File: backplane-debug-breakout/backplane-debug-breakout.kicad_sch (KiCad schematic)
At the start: 11 parts, among them J1 Conn_02x08_Odd_Even, J2 Conn_01x04, J3 Conn_01x01_Socket, J4 Conn_01x01_Socket, J5 Conn_01x04, SW1 SW_Push, SW2 SW_DPST_x2, U1 UMFT234XF

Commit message: modified pcb
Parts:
- removed SW1: SW_Push, oresat-misc:D6R90_CNK, symbol Switch:SW_Push
- removed SW2: SW_DPST_x2, Connector_PinHeader_2.54mm:PinHeader_1x03_P2.54mm_Vertical, symbol Switch:SW_DPST_x2
- added SW2: SW_Omron_B3FS, Button_Switch_THT:SW_PUSH_6mm, symbol Switch:SW_Omron_B3FS
- added SW3: EG1218, Connector_PinHeader_2.54mm:PinHeader_1x03_P2.54mm_Vertical, symbol Switch:SW_SPDT_321
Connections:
- net GND: now also SW2.1, SW3.1 (C)
- net SD: now also SW2.2, SW3.2 (B)
- net VBUS: now reaches F1.1, J1.10 (Pin_10), J1.6 (Pin_6), J1.8 (Pin_8)
- no-connect marks 8 -> 11
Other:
- note added: "Banana jacks for external power"
- note added: "Oresat backplane 16-pin connector"
- note added: "USB to UART adapter daughterboard to debug pc via micro-usb"
- note added: "add spacing to pins"
- note added: "momentary button and slide switch for ~{SHUTDOWN}"
- note added: "not used"
- note added: "vulCAN USB to CAN adapter to debug pc via USB-C"
- note removed: "To vulCAN"
- note removed: "check switch footprints"
- title: (none) -> Backplane Debug Breakout
- moved on the sheet: D1, F1, F2, J1, J2, J3, J4, J5, U1

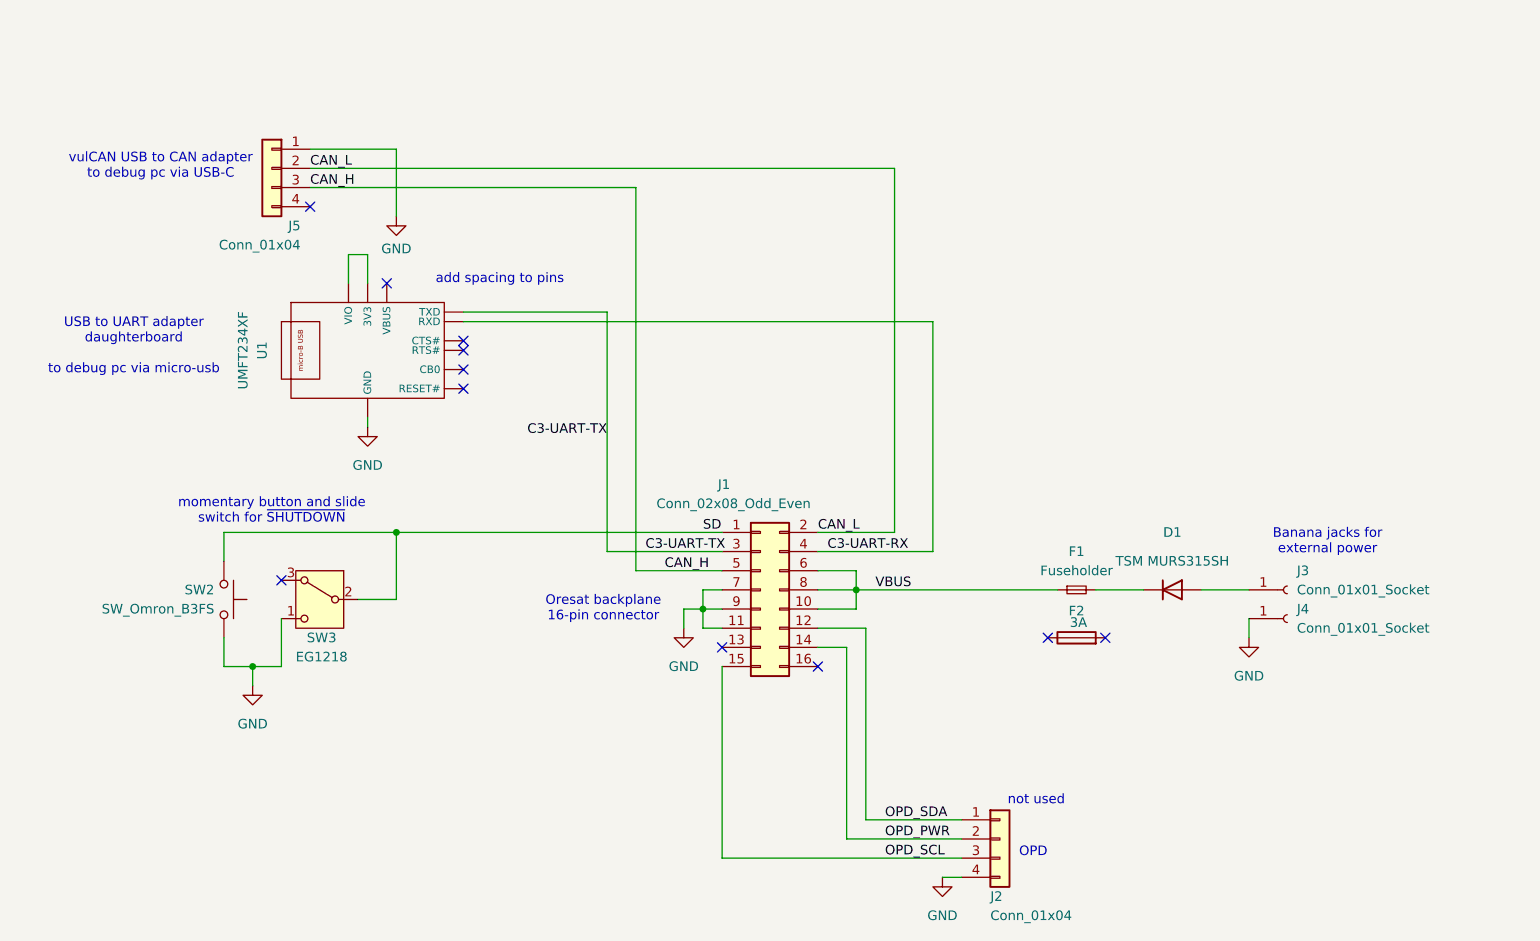
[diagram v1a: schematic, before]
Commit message: Random clean, including some value changes, and moving the vulcan connector around to minimize wire lengths.
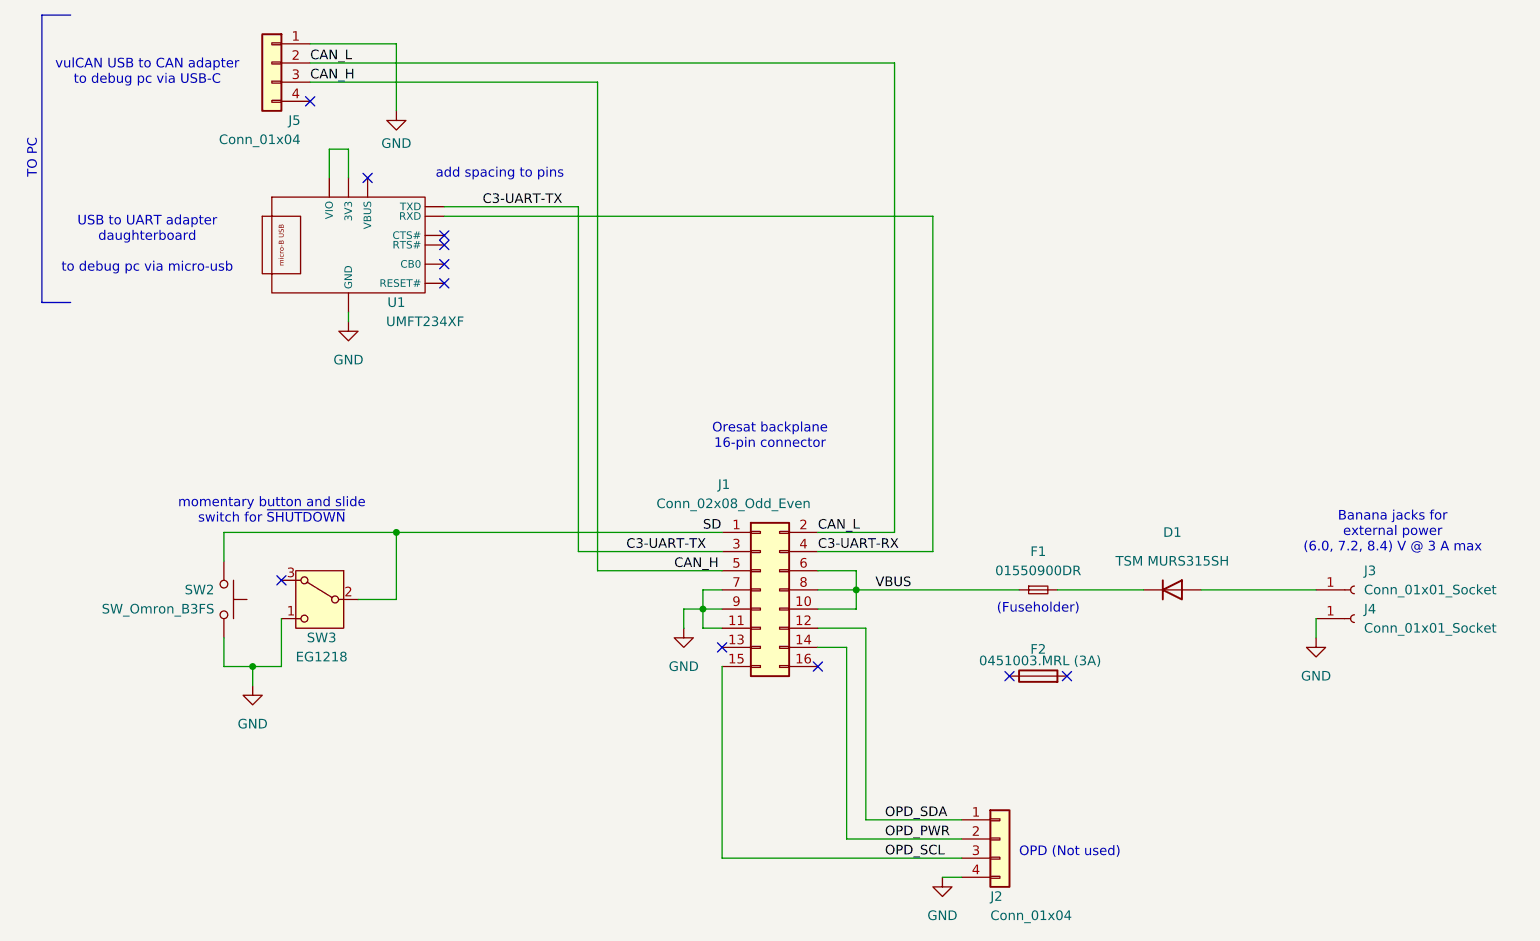
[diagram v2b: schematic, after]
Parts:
- F1: value Fuseholder -> 01550900DR
- F2: value 3A -> 0451003.MRL (3A)
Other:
- note added: "(Fuseholder)"
- note added: "Banana jacks for external power (6.0, 7.2, 8.4) V @ 3 A max"
- note added: "OPD (Not used)"
- note added: "TO PC"
- note removed: "Banana jacks for external power"
- note removed: "OPD"
- note removed: "not used"
- moved on the sheet: F1, F2, J3, J4, J5, U1

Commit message: updated BOM
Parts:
- D1: DST (none) -> Digi-Key; MFR (none) -> TSM
- F1, F2: DST (none) -> Digi-Key; MFR (none) -> LittelFuse
- J1: DPN 609-86130161014345E1LF-ND -> H3DDH-1611618G-ND; DST (none) -> Digi-Key; MFR (none) -> Assman; MPN 86130161014345E1LF -> H3DDH-161618G
- J2: DST (none) -> Digi-Key; now not fitted; now left out of the parts list
- J3: DPN (none) -> 36-7006-ND; DST (none) -> Digi-Key; MFR (none) -> KEYSTONE; MPN (none) -> 7006
- J4: DPN (none) -> 36-7007-ND; DST (none) -> Digi-Key; MFR (none) -> KEYSTONE; MPN (none) -> 7007
- J5: DST (none) -> Digi-Key
- SW2: DPN (none) -> SW400-ND; DST (none) -> Digi-Key; MFR (none) -> Omron; MPN (none) -> B3F-1000
- SW3: DPN (none) -> EG1903-ND; DST (none) -> Digi-Key; MFR (none) -> E-Switch; MPN (none) -> EG1218
- U1: DST (none) -> Digi-Key; MFR (none) -> FTDI, Future Technology Devices International Ltd

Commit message: edited BOM
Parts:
- J1: DPN H3DDH-1611618G-ND -> 732-2095-ND; MFR Assman -> Würth Elektronik; MPN H3DDH-161618G -> 61201621621
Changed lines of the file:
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@@
 			)
 		)
-		(property "Description" "16-position cable assembly socket"
+		(property "Description" "CONN HEADER VERT 16POS 2.54MM Y - 0"
 			(at 144.78 97.79 0)
 			(effects
@@
 			)
 		)
-		(property "DPN" "H3DDH-1611618G-ND"
+		(property "DPN" "732-2095-ND"
 			(at 144.78 97.79 0)
 			(effects
@@
 			)
 		)
-		(property "MPN" "H3DDH-161618G"
+		(property "MPN" "61201621621"
 			(at 144.78 97.79 0)
 			(effects
@@
 			)
 		)
-		(property "MFR" "Assman"
+		(property "MFR" "Würth Elektronik"
 			(at 144.78 97.79 0)
 			(effects

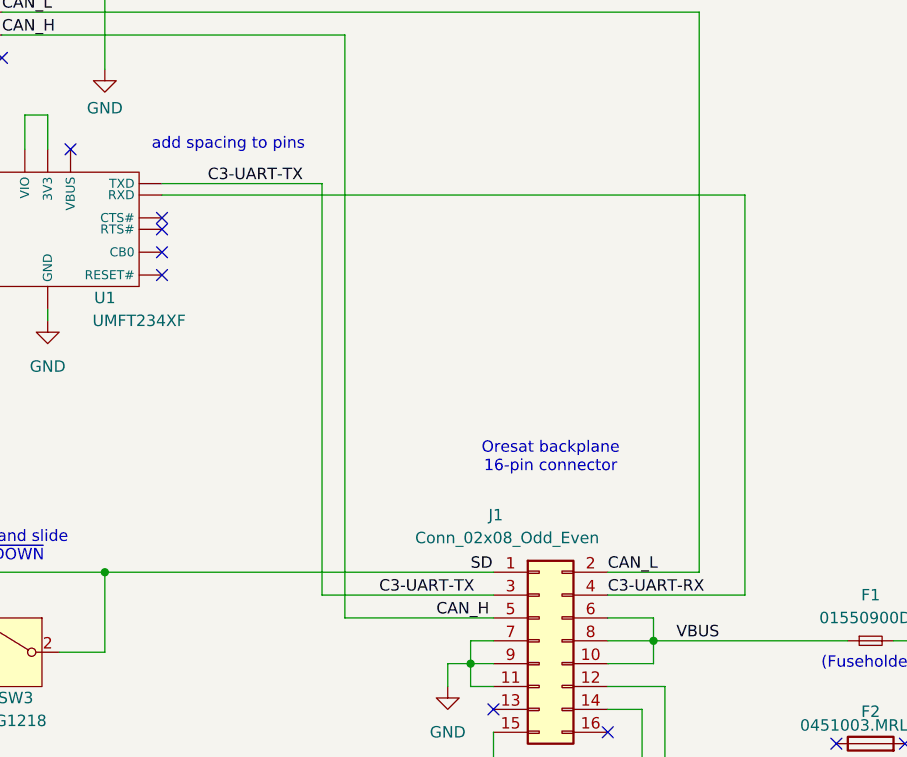
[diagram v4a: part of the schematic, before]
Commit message: fixed tx-rx connections
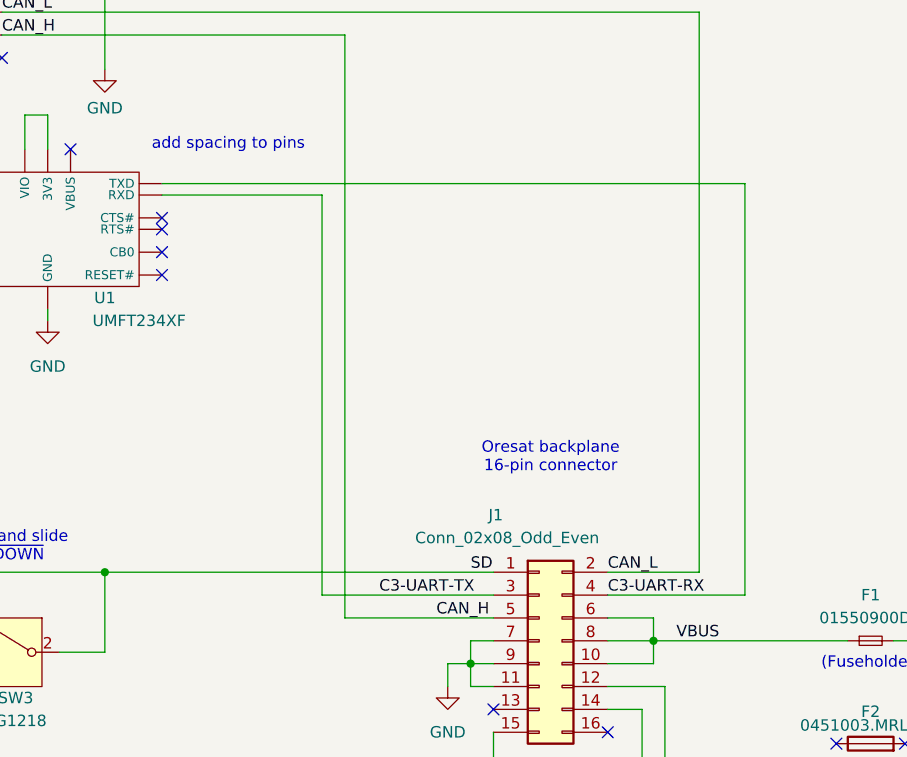
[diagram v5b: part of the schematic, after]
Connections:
- net C3-UART-RX: now also U1.P7 (TXD); no longer U1.P9 (RXD)
- net C3-UART-TX: now also U1.P9 (RXD); no longer U1.P7 (TXD)
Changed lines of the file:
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@@
 	(wire
 		(pts
-			(xy 120.65 46.99) (xy 120.65 92.71)
+			(xy 167.64 46.99) (xy 102.87 46.99)
+		)
+		(stroke
+			(width 0)
+			(type default)
+		)
+	)
+	(wire
+		(pts
+			(xy 120.65 48.26) (xy 102.87 48.26)
 		)
 		(stroke
@@
 	(wire
 		(pts
-			(xy 102.87 46.99) (xy 120.65 46.99)
-		)
-		(stroke
-			(width 0)
-			(type default)
-		)
-	)
-	(wire
-		(pts
 			(xy 137.16 100.33) (xy 137.16 102.87)
 		)
@@
 	(wire
 		(pts
+			(xy 120.65 92.71) (xy 120.65 48.26)
+		)
+		(stroke
+			(width 0)
+			(type default)
+		)
+	)
+	(wire
+		(pts
 			(xy 168.91 135.89) (xy 171.45 135.89)
 		)
@@
 	(wire
 		(pts
-			(xy 167.64 48.26) (xy 102.87 48.26)
-		)
-		(stroke
-			(width 0)
-			(type default)
-		)
-	)
-	(wire
-		(pts
 			(xy 162.56 90.17) (xy 162.56 27.94)
 		)
@@
 	(wire
 		(pts
-			(xy 167.64 92.71) (xy 167.64 48.26)
+			(xy 167.64 46.99) (xy 167.64 92.71)
 		)
 		(stroke
@@
 		(fields_autoplaced yes)
 		(effects
-			(font
-				(size 1.27 1.27)
-			)
-			(justify left bottom)
-		)
-	)
-	(label "C3-UART-TX"
-		(at 107.95 46.99 0)
-		(fields_autoplaced yes)
-		(effects

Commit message: updated schematic
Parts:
- added C1: C, symbol Device:C
- added J6: 629105150521, Connector_USB:USB_Micro-B_Wuerth_629105150521_CircularHoles, symbol Connector:USB_B_Micro
- added SW1: SW_Push_DPDT, symbol Switch:SW_Push_DPDT
- added TP1: TestPoint, symbol Connector:TestPoint
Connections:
- net C3-UART-RX: now also SW1.5 (B); no longer U1.P7 (TXD)
- net C3-UART-TX: now also SW1.2 (B); no longer U1.P9 (RXD)
- net GND: now also C1.2, J6.5 (GND)
- new net: SW1.1 (A), U1.P9 (RXD)
- new net: J6.2 (D-), SW1.3 (C)
- new net: SW1.4 (A), U1.P7 (TXD)
- new net: J6.3 (D+), SW1.6 (C)
- new net: C1.1, J6.6 (Shield)
- new net: J6.1 (VBUS), TP1.1
- no-connect marks 11 -> 12

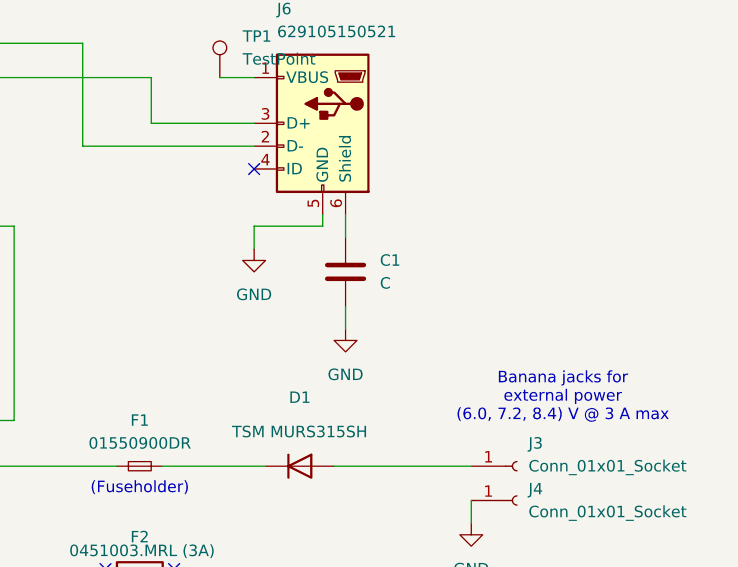
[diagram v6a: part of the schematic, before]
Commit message: added usb-serial connector to schematic and pcb
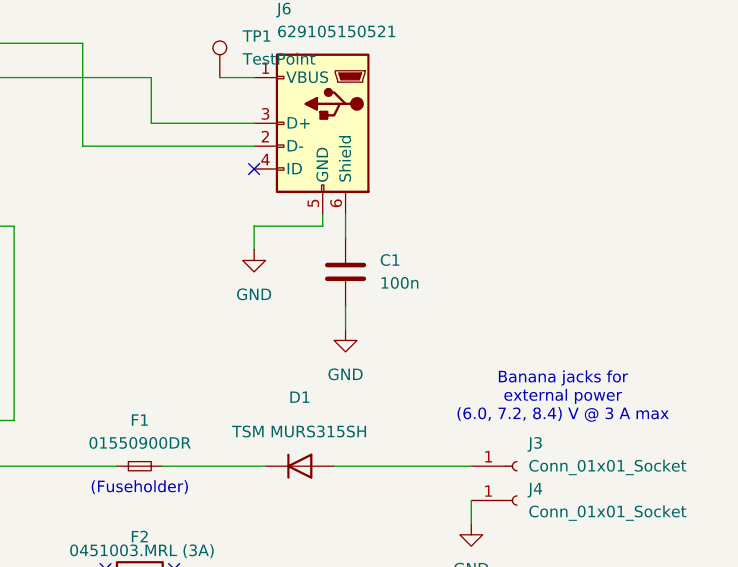
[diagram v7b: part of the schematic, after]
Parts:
- C1: value C -> 100n; footprint (none) -> Capacitor_SMD:C_0603_1608Metric
- SW1: footprint (none) -> oresat-passives:DPDT slide switch 6 pin
- TP1: footprint (none) -> oresat-misc:TestPoint-0.75mm-th
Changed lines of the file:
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@@
 			)
 		)
-		(property "Footprint" ""
+		(property "Footprint" "oresat-passives:DPDT slide switch 6 pin"
 			(at 135.89 59.69 0)
 			(effects
@@
 			)
 		)
-		(property "Value" "C"
+		(property "Value" "100n"
 			(at 208.28 77.4699 0)
 			(effects
@@
 			)
 		)
-		(property "Footprint" ""
+		(property "Footprint" "Capacitor_SMD:C_0603_1608Metric"
 			(at 205.4352 80.01 0)
 			(effects
@@
 			)
 		)
-		(property "Footprint" ""
+		(property "Footprint" "oresat-misc:TestPoint-0.75mm-th"
 			(at 195.58 54.61 0)
 			(effects

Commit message: made changes to layout of pcb
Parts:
- removed J3, J4: Conn_01x01_Socket, Connector:Banana_Jack_1Pin, symbol Connector:Conn_01x01_Socket
- added J4: Conn_01x02_Socket, oresat-connectors:PHOENIX_1995499, symbol Connector:Conn_01x02_Socket
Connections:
- net GND: now also J4.2 (Pin_2)
- net at D1.2 (A): now also J4.1 (Pin_1)
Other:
- note removed: "Banana jacks for external power (6.0, 7.2, 8.4) V @ 3 A max"
